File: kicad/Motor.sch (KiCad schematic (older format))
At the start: 5 parts, among them P2 Motor_L, P3 Motor_R, U4 DRV8835

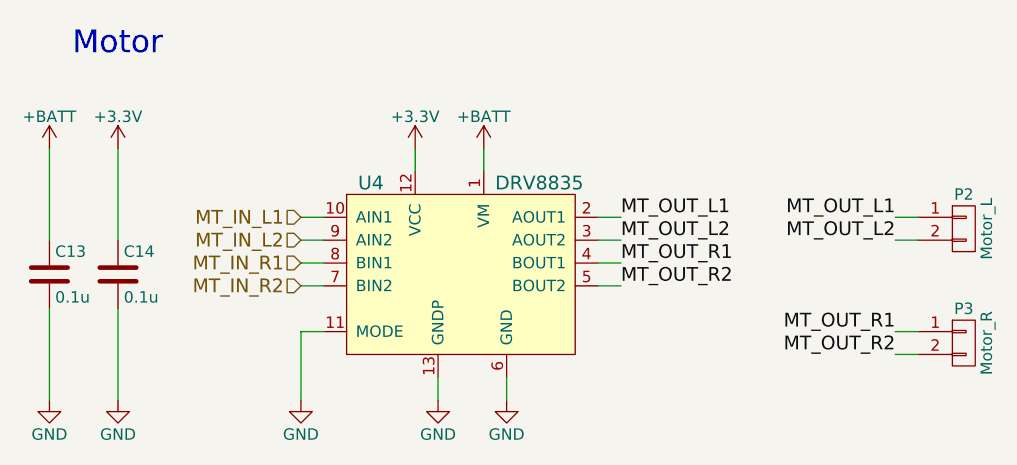
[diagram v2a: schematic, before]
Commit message: 回路とフットプリントを改良
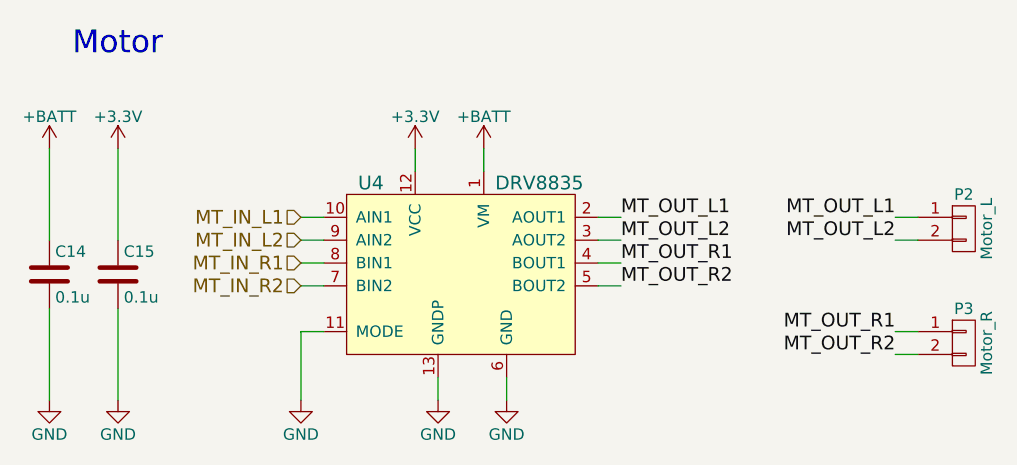
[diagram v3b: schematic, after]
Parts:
- renumbered C13 to C14, C14 to C15
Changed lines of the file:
@@
 	5600 3100 5600 3200
 $Comp
-L GND #PWR014
+L GND #PWR015
 U 1 1 57CA1E38
 P 5400 4200
-F 0 "#PWR014" H 5400 3950 50  0001 C CNN
+F 0 "#PWR015" H 5400 3950 50  0001 C CNN
 F 1 "GND" H 5400 4050 50  0000 C CNN
 F 2 "" H 5400 4200 50  0000 C CNN
@@
 	5400 4200 5400 4100
 $Comp
-L GND #PWR015
+L GND #PWR016
 U 1 1 57CA1E3F
 P 5700 4200
-F 0 "#PWR015" H 5700 3950 50  0001 C CNN
+F 0 "#PWR016" H 5700 3950 50  0001 C CNN
 F 1 "GND" H 5700 4050 50  0000 C CNN
 F 2 "" H 5700 4200 50  0000 C CNN
@@
 	5700 4200 5700 4100
 $Comp
-L GND #PWR016
+L GND #PWR017
 U 1 1 57CA1E46
 P 4800 4200
-F 0 "#PWR016" H 4800 3950 50  0001 C CNN
+F 0 "#PWR017" H 4800 3950 50  0001 C CNN
 F 1 "GND" H 4800 4050 50  0000 C CNN
 F 2 "" H 4800 4200 50  0000 C CNN
@@
 Motor
 $Comp
-L C C14
+L C C15
 U 1 1 57CCEFE0
 P 4000 3650
-F 0 "C14" H 4025 3750 50  0000 L CNN
+F 0 "C15" H 4025 3750 50  0000 L CNN
 F 1 "0.1u" H 4025 3550 50  0000 L CNN
 F 2 "Capacitors_SMD:C_0201" H 4038 3500 50  0001 C CNN
@@
 $EndComp
 $Comp
-L GND #PWR017
+L GND #PWR018
 U 1 1 57CCF046
 P 4000 4200
-F 0 "#PWR017" H 4000 3950 50  0001 C CNN
+F 0 "#PWR018" H 4000 3950 50  0001 C CNN
 F 1 "GND" H 4000 4050 50  0000 C CNN
 F 2 "" H 4000 4200 50  0000 C CNN
@@
 	4000 3800 4000 4200
 $Comp
-L +BATT #PWR018
+L +BATT #PWR019
 U 1 1 57CD5BEE
 P 5600 3100
-F 0 "#PWR018" H 5600 2950 50  0001 C CNN
+F 0 "#PWR019" H 5600 2950 50  0001 C CNN
 F 1 "+BATT" H 5600 3240 50  0000 C CNN
 F 2 "" H 5600 3100 50  0000 C CNN
@@
 	7500 3500 7400 3500
 $Comp
-L +3.3V #PWR019
+L +3.3V #PWR020
 U 1 1 589CC6A5
 P 5300 3100
-F 0 "#PWR019" H 5300 2950 50  0001 C CNN
+F 0 "#PWR020" H 5300 2950 50  0001 C CNN
 F 1 "+3.3V" H 5300 3240 50  0000 C CNN
 F 2 "" H 5300 3100 50  0000 C CNN
@@
 $EndComp
 $Comp
-L +3.3V #PWR020
+L +3.3V #PWR021
 U 1 1 589CC6C6
 P 4000 3100
-F 0 "#PWR020" H 4000 2950 50  0001 C CNN
+F 0 "#PWR021" H 4000 2950 50  0001 C CNN
 F 1 "+3.3V" H 4000 3240 50  0000 C CNN
 F 2 "" H 4000 3100 50  0000 C CNN
@@
 $EndComp
 $Comp
-L +BATT #PWR021
+L +BATT #PWR022
 U 1 1 594721DF
 P 3700 3100
-F 0 "#PWR021" H 3700 2950 50  0001 C CNN
+F 0 "#PWR022" H 3700 2950 50  0001 C CNN
 F 1 "+BATT" H 3700 3240 50  0000 C CNN
 F 2 "" H 3700 3100 50  0000 C CNN
@@
 $EndComp
 $Comp
-L C C13
+L C C14
 U 1 1 594721FA
 P 3700 3650
-F 0 "C13" H 3725 3750 50  0000 L CNN
+F 0 "C14" H 3725 3750 50  0000 L CNN
 F 1 "0.1u" H 3725 3550 50  0000 L CNN
 F 2 "Capacitors_SMD:C_0201" H 3738 3500 50  0001 C CNN
@@
 $EndComp
 $Comp
-L GND #PWR022
+L GND #PWR023
 U 1 1 59472221
 P 3700 4200
-F 0 "#PWR022" H 3700 3950 50  0001 C CNN
+F 0 "#PWR023" H 3700 3950 50  0001 C CNN
 F 1 "GND" H 3700 4050 50  0000 C CNN
 F 2 "" H 3700 4200 50  0000 C CNN

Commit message: 自動配線1残し
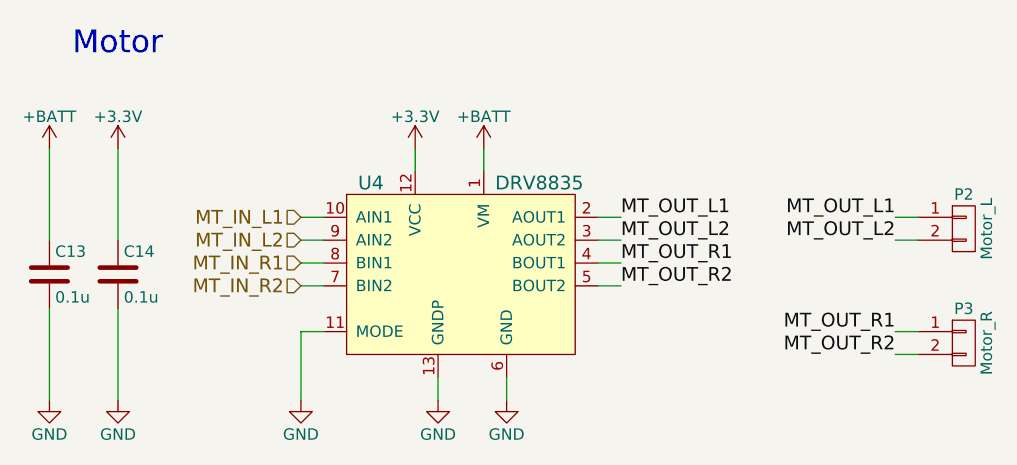
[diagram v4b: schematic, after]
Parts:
- renumbered C14 to C13, C15 to C14
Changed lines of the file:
@@
 Motor
 $Comp
-L C C15
+L C C14
 U 1 1 57CCEFE0
 P 4000 3650
-F 0 "C15" H 4025 3750 50  0000 L CNN
+F 0 "C14" H 4025 3750 50  0000 L CNN
 F 1 "0.1u" H 4025 3550 50  0000 L CNN
 F 2 "Capacitors_SMD:C_0201" H 4038 3500 50  0001 C CNN
@@
 $EndComp
 $Comp
-L C C14
+L C C13
 U 1 1 594721FA
 P 3700 3650
-F 0 "C14" H 3725 3750 50  0000 L CNN
+F 0 "C13" H 3725 3750 50  0000 L CNN
 F 1 "0.1u" H 3725 3550 50  0000 L CNN
 F 2 "Capacitors_SMD:C_0201" H 3738 3500 50  0001 C CNN

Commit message: 実装経験をもとにフットプリントを改良，ミスを修正
SC70サイズのオペアンプのピンアサインを修正
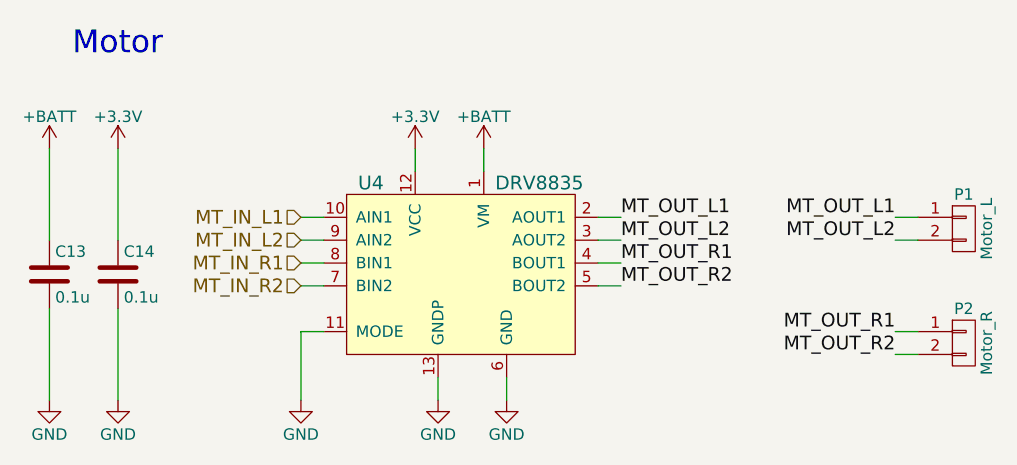
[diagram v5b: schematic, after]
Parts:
- renumbered P2 to P1, P3 to P2
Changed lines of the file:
@@
 	5600 3100 5600 3200
 $Comp
-L GND #PWR015
+L GND #PWR21
 U 1 1 57CA1E38
 P 5400 4200
-F 0 "#PWR015" H 5400 3950 50  0001 C CNN
+F 0 "#PWR21" H 5400 3950 50  0001 C CNN
 F 1 "GND" H 5400 4050 50  0000 C CNN
 F 2 "" H 5400 4200 50  0000 C CNN
@@
 	5400 4200 5400 4100
 $Comp
-L GND #PWR016
+L GND #PWR23
 U 1 1 57CA1E3F
 P 5700 4200
-F 0 "#PWR016" H 5700 3950 50  0001 C CNN
+F 0 "#PWR23" H 5700 3950 50  0001 C CNN
 F 1 "GND" H 5700 4050 50  0000 C CNN
 F 2 "" H 5700 4200 50  0000 C CNN
@@
 	5700 4200 5700 4100
 $Comp
-L GND #PWR017
+L GND #PWR19
 U 1 1 57CA1E46
 P 4800 4200
-F 0 "#PWR017" H 4800 3950 50  0001 C CNN
+F 0 "#PWR19" H 4800 3950 50  0001 C CNN
 F 1 "GND" H 4800 4050 50  0000 C CNN
 F 2 "" H 4800 4200 50  0000 C CNN
@@
 $EndComp
 $Comp
-L GND #PWR018
+L GND #PWR18
 U 1 1 57CCF046
 P 4000 4200
-F 0 "#PWR018" H 4000 3950 50  0001 C CNN
+F 0 "#PWR18" H 4000 3950 50  0001 C CNN
 F 1 "GND" H 4000 4050 50  0000 C CNN
 F 2 "" H 4000 4200 50  0000 C CNN
@@
 	4000 3800 4000 4200
 $Comp
-L +BATT #PWR019
+L +BATT #PWR22
 U 1 1 57CD5BEE
 P 5600 3100
-F 0 "#PWR019" H 5600 2950 50  0001 C CNN
+F 0 "#PWR22" H 5600 2950 50  0001 C CNN
 F 1 "+BATT" H 5600 3240 50  0000 C CNN
 F 2 "" H 5600 3100 50  0000 C CNN
@@
 	4900 3700 4800 3700
 $Comp
-L CONN_01X02 P2
+L CONN_01X02 P1
 U 1 1 589D679E
 P 7700 3450
-F 0 "P2" H 7700 3600 50  0000 C CNN
+F 0 "P1" H 7700 3600 50  0000 C CNN
 F 1 "Motor_L" V 7800 3450 50  0000 C CNN
 F 2 "mouse:SMD_conn_2" H 7700 3450 50  0001 C CNN
@@
 $EndComp
 $Comp
-L CONN_01X02 P3
+L CONN_01X02 P2
 U 1 1 589D680E
 P 7700 3950
-F 0 "P3" H 7700 4100 50  0000 C CNN
+F 0 "P2" H 7700 4100 50  0000 C CNN
 F 1 "Motor_R" V 7800 3950 50  0000 C CNN
 F 2 "mouse:SMD_conn_2" H 7700 3950 50  0001 C CNN
@@
 	7500 3500 7400 3500
 $Comp
-L +3.3V #PWR020
+L +3.3V #PWR20
 U 1 1 589CC6A5
 P 5300 3100
-F 0 "#PWR020" H 5300 2950 50  0001 C CNN
+F 0 "#PWR20" H 5300 2950 50  0001 C CNN
 F 1 "+3.3V" H 5300 3240 50  0000 C CNN
 F 2 "" H 5300 3100 50  0000 C CNN
@@
 $EndComp
 $Comp
-L +3.3V #PWR021
+L +3.3V #PWR17
 U 1 1 589CC6C6
 P 4000 3100
-F 0 "#PWR021" H 4000 2950 50  0001 C CNN
+F 0 "#PWR17" H 4000 2950 50  0001 C CNN
 F 1 "+3.3V" H 4000 3240 50  0000 C CNN
 F 2 "" H 4000 3100 50  0000 C CNN
@@
 $EndComp
 $Comp
-L +BATT #PWR022
+L +BATT #PWR15
 U 1 1 594721DF
 P 3700 3100
-F 0 "#PWR022" H 3700 2950 50  0001 C CNN
+F 0 "#PWR15" H 3700 2950 50  0001 C CNN
 F 1 "+BATT" H 3700 3240 50  0000 C CNN
 F 2 "" H 3700 3100 50  0000 C CNN
@@
 $EndComp
 $Comp
-L GND #PWR023
+L GND #PWR16
 U 1 1 59472221
 P 3700 4200
-F 0 "#PWR023" H 3700 3950 50  0001 C CNN
+F 0 "#PWR16" H 3700 3950 50  0001 C CNN
 F 1 "GND" H 3700 4050 50  0000 C CNN
 F 2 "" H 3700 4200 50  0000 C CNN
